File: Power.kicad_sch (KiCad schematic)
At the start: 0 parts

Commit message: added  power components
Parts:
- added U2: LM2776, Package_TO_SOT_SMD:SOT-23-6, symbol Regulator_SwitchedCapacitor:LM2776
- added U5: LM337L_SO8, Package_SO:SOIC-8_3.9x4.9mm_P1.27mm, symbol Regulator_Linear:LM337L_SO8
- added U6: LM1117MP-3.3, Package_TO_SOT_SMD:SOT-223-3_TabPin2, symbol Regulator_Linear:LM1117MP-3.3
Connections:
- new net: U5.2 (VI), U5.3 (VI), U5.6 (VI), U5.7 (VI)
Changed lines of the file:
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@@
 	(generator_version "8.0")
 	(paper "A4")
+	(symbol
+		(lib_id "Regulator_Linear:LM337L_SO8")
+		(at 139.7 92.71 0)
+		(unit 1)
+		(exclude_from_sim no)
+		(in_bom yes)
+		(on_board yes)
+		(dnp no)
+		(fields_autoplaced yes)
+		(property "Reference" "U5"
+			(at 139.7 96.52 0)
+			(effects
+				(font
+					(size 1.27 1.27)
+				)
+			)
+		)
+		(property "Value" "LM337L_SO8"
+			(at 139.7 99.06 0)
+			(effects
+				(font
+					(size 1.27 1.27)
+				)
+			)
+		)
+		(property "Footprint" "Package_SO:SOIC-8_3.9x4.9mm_P1.27mm"
+			(at 139.7 97.79 0)
+			(effects
+				(font
+					(size 1.27 1.27)
+					(italic yes)
+				)
+				(hide yes)
+			)
+		)
+		(property "Datasheet" "http://www.ti.com/lit/ds/symlink/lm337l.pdf"
+			(at 139.7 92.71 0)
+			(effects
+				(font
+					(size 1.27 1.27)
+				)
+				(hide yes)
+			)
+		)
+		(property "Description" "100mA 35V Adjustable Negative Linear Regulator, SO-8"
+			(at 139.7 92.71 0)
+			(effects
+				(font
+					(size 1.27 1.27)
+				)
+				(hide yes)
+			)
+		)
+		(pin "3"
+		)
+		(pin "4"
+		)
+		(pin "2"
+		)
+		(pin "6"
+		)
+		(pin "7"
+		)
+		(pin "8"
+		)
+		(pin "1"
+		)
+		(pin "5"
+		)
+		(instances
+			(project "STM32_Play_Board"
+				(path "/9848a691-cd53-4e57-940a-e5db2e63f9a1/fed4e8b7-2c37-42f6-8803-c612b1069bda"
+					(reference "U5")
+					(unit 1)
+				)
+			)
+		)
+	)
+	(symbol
+		(lib_id "Regulator_Linear:LM1117MP-3.3")
+		(at 99.06 58.42 0)
+		(unit 1)
+		(exclude_from_sim no)
+		(in_bom yes)
+		(on_board yes)
+		(dnp no)
+		(fields_autoplaced yes)
+		(property "Reference" "U6"
+			(at 99.06 52.07 0)
+			(effects
+				(font
+					(size 1.27 1.27)
+				)
+			)
+		)
+		(property "Value" "LM1117MP-3.3"
+			(at 99.06 54.61 0)
+			(effects
+				(font
+					(size 1.27 1.27)
+				)
+			)
+		)
+		(property "Footprint" "Package_TO_SOT_SMD:SOT-223-3_TabPin2"
+			(at 99.06 58.42 0)
+			(effects
+				(font
+					(size 1.27 1.27)
+				)
+				(hide yes)
+			)
+		)
+		(property "Datasheet" "http://www.ti.com/lit/ds/symlink/lm1117.pdf"
+			(at 99.06 58.42 0)
+			(effects
+				(font
+					(size 1.27 1.27)
+				)
+				(hide yes)
+			)
+		)
+		(property "Description" "800mA Low-Dropout Linear Regulator, 3.3V fixed output, SOT-223"
+			(at 99.06 58.42 0)
+			(effects
+				(font
+					(size 1.27 1.27)
+				)
+				(hide yes)
+			)
+		)
+		(pin "1"
+		)
+		(pin "2"
+		)
+		(pin "3"
+		)
+		(instances
+			(project "STM32_Play_Board"
+				(path "/9848a691-cd53-4e57-940a-e5db2e63f9a1/fed4e8b7-2c37-42f6-8803-c612b1069bda"
+					(reference "U6")
+					(unit 1)
+				)
+			)
+		)
+	)
+	(symbol
+		(lib_id "Regulator_SwitchedCapacitor:LM2776")
+		(at 105.41 92.71 0)
+		(unit 1)
+		(exclude_from_sim no)
+		(in_bom yes)
+		(on_board yes)
+		(dnp no)
+		(fields_autoplaced yes)
+		(property "Reference" "U2"
+			(at 118.11 83.8514 0)
+			(effects
+				(font
+					(size 1.27 1.27)
+				)
+			)
+		)
+		(property "Value" "LM2776"
+			(at 118.11 86.3914 0)
+			(effects
+				(font
+					(size 1.27 1.27)
+				)
+			)
+		)
+		(property "Footprint" "Package_TO_SOT_SMD:SOT-23-6"
+			(at 106.68 101.6 0)
+			(effects
+				(font
+					(size 1.27 1.27)
+				)
+				(justify left)
+				(hide yes)
+			)
+		)
+		(property "Datasheet" "http://www.ti.com/lit/ds/symlink/lm2776.pdf"
+			(at 58.42 60.96 0)
+			(effects
+				(font
+					(size 1.27 1.27)
+				)
+				(hide yes)
+			)
+		)
+		(property "Description" "Switched capacitor inverter, inverts positive voltage +2.7 to +5.5V to negative, 200mA, SOT-23-6"
+			(at 105.41 92.71 0)
+			(effects
+				(font
+					(size 1.27 1.27)
+				)
+				(hide yes)
+			)
+		)
+		(pin "1"
+		)
+		(pin "2"
+		)
+		(pin "3"
+		)
+		(pin "5"
+		)
+		(pin "4"
+		)
+		(pin "6"
+		)
+		(instances
+			(project "STM32_Play_Board"
+				(path "/9848a691-cd53-4e57-940a-e5db2e63f9a1/fed4e8b7-2c37-42f6-8803-c612b1069bda"
+					(reference "U2")
+					(unit 1)
+				)
+			)
+		)
+	)
 )

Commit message: dfvdfv
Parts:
- removed U5: LM337L_SO8, Package_SO:SOIC-8_3.9x4.9mm_P1.27mm, symbol Regulator_Linear:LM337L_SO8
- added C15, C16, C18, C6: 10 uF, symbol Device:C
- added C17: 1 uF, symbol Device:C
- added C7: 4.7 uF, symbol Device:C
- added J5, J6: Conn_01x01_Pin, symbol Connector:Conn_01x01_Pin
- added JP1, JP2: Jumper_2_Open, symbol Jumper:Jumper_2_Open
- added R10: 400, symbol Device:R_US
- added R9: 240, symbol Device:R_US
- added U7: LM337L_SO8, Package_SO:SOIC-8_3.9x4.9mm_P1.27mm, symbol Regulator_Linear:LM337L_SO8
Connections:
- net Earth: now reaches U6.1 (GND)
- net Earth: now also U2.2 (GND), C16.2, C17.2, C18.1, C6.2, C7.2, J5.1 (Pin_1), R10.1
- net +3.3V: now reaches U6.2 (VO)
- net +3.3V: now also U2.3 (VIN), U2.4 (EN), C17.1, C6.1
- net at U6.3 (VI): now also C7.1, JP1.2 (B), JP2.2 (B)
- net at U2.1 (VOUT): now also C16.1, U7.2 (VI), U7.3 (VI), U7.6 (VI), U7.7 (VI)
- net at U2.5 (C1+): now also C15.1
- net at U2.6 (C1-): now also C15.2
- new net: J6.1 (Pin_1), JP2.1 (A)
- new net: C18.2, R9.2, U7.1 (VO)
- new net: R10.2, R9.1, U7.4 (ADJ)
- new net VBUS: JP1.1 (A)
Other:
- moved on the sheet: U2, U6

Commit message: added voltage measurement and current measurement
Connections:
- net -3V3: now reaches C18.2, R9.2, U7.1 (VO)
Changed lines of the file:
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@@
+	)
+	(junction
+		(at 214.63 113.03)
+		(diameter 0)
+		(color 0 0 0 0)
 	)
 	(junction
@@
 		(pts
 			(xy 137.16 82.55) (xy 137.16 105.41)
+		)
+		(stroke
+			(width 0)
+			(type default)
+		)
+	)
+	(wire
+		(pts
+			(xy 214.63 113.03) (xy 214.63 120.65)
 		)
 		(stroke
@@
 					(unit 1)
 				)
+			)
+		)
+	)
+	(symbol
+		(lib_id "power:-3V3")
+		(at 214.63 120.65 180)
+		(unit 1)
+		(exclude_from_sim no)
+		(in_bom yes)
+		(on_board yes)
+		(dnp no)
+		(fields_autoplaced yes)
+		(property "Reference" "#PWR033"
+			(at 214.63 116.84 0)
+			(effects
+				(font
+					(size 1.27 1.27)
+				)
+				(hide yes)
+			)
+		)
+		(property "Value" "-3V3"
+			(at 214.63 125.73 0)
+			(effects
+				(font
+					(size 1.27 1.27)
+				)
+			)
+		)
+		(property "Footprint" ""
+			(at 214.63 120.65 0)
+			(effects
+				(font
+					(size 1.27 1.27)
+				)
+				(hide yes)
+			)
+		)
+		(property "Datasheet" ""
+			(at 214.63 120.65 0)
+			(effects
+				(font
+					(size 1.27 1.27)
+				)
+				(hide yes)
+			)
+		)
+		(property "Description" "Power symbol creates a global label with name \"-3V3\""
+			(at 214.63 120.65 0)
+			(effects
+				(font
+					(size 1.27 1.27)
+				)
+				(hide yes)
+			)
+		)
+		(pin "1"
+		)
+		(instances
+			(project "STM32_Play_Board"
+				(path "/9848a691-cd53-4e57-940a-e5db2e63f9a1/fed4e8b7-2c37-42f6-8803-c612b1069bda"
+					(reference "#PWR033")
+					(unit 1)
+				)

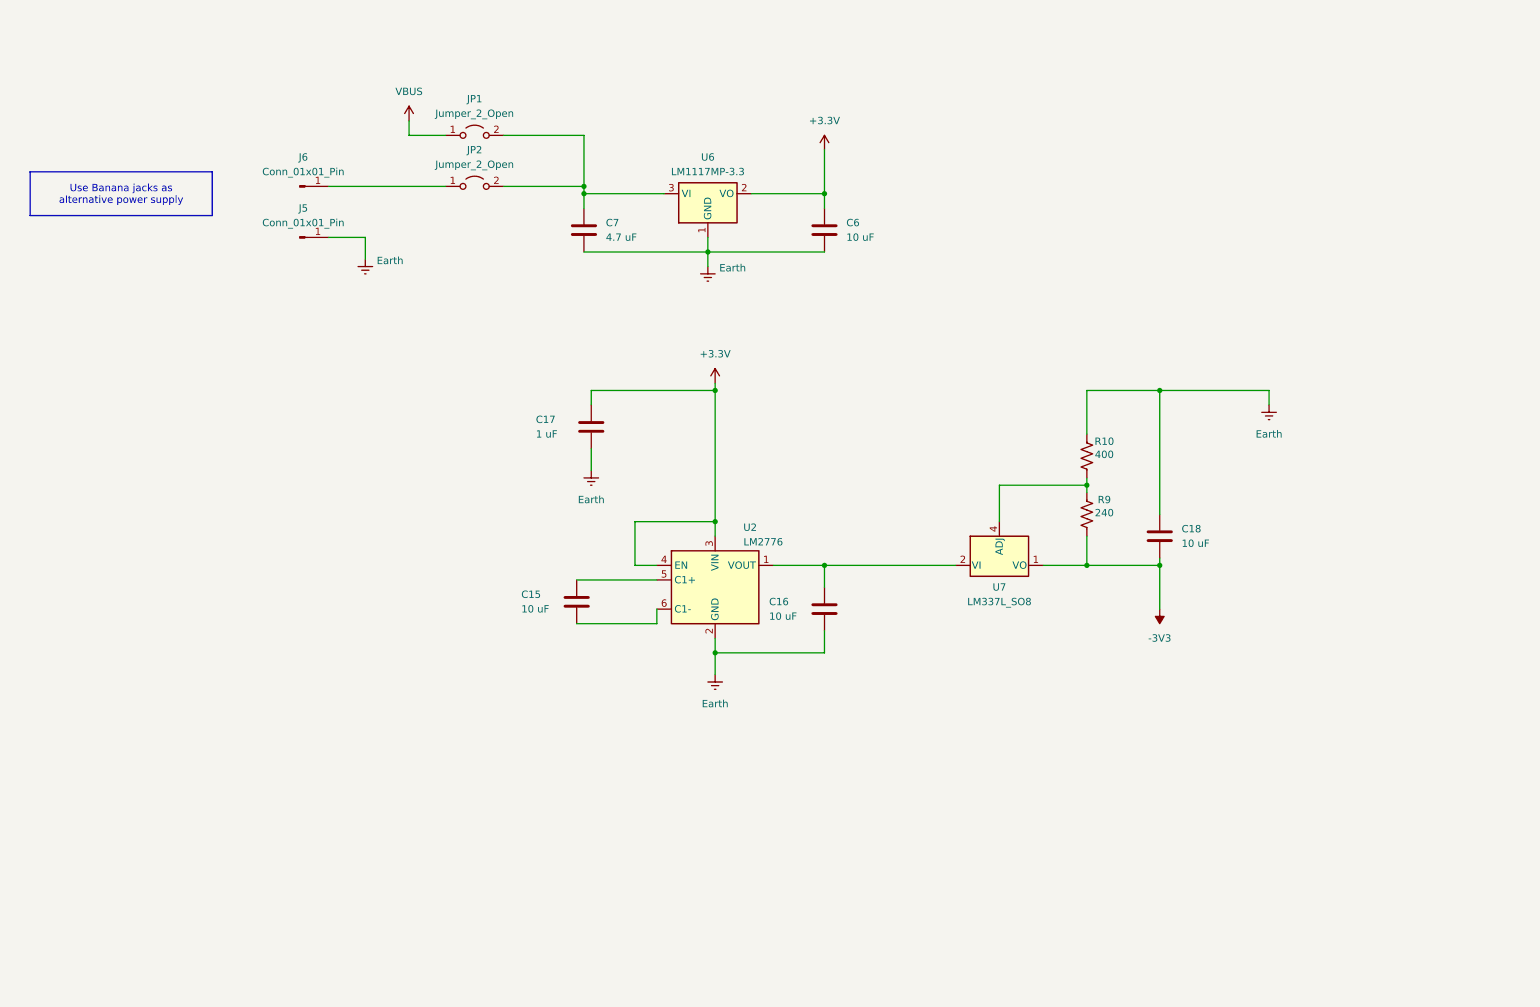
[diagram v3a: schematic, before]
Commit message: updated schematics added the stm cube project file
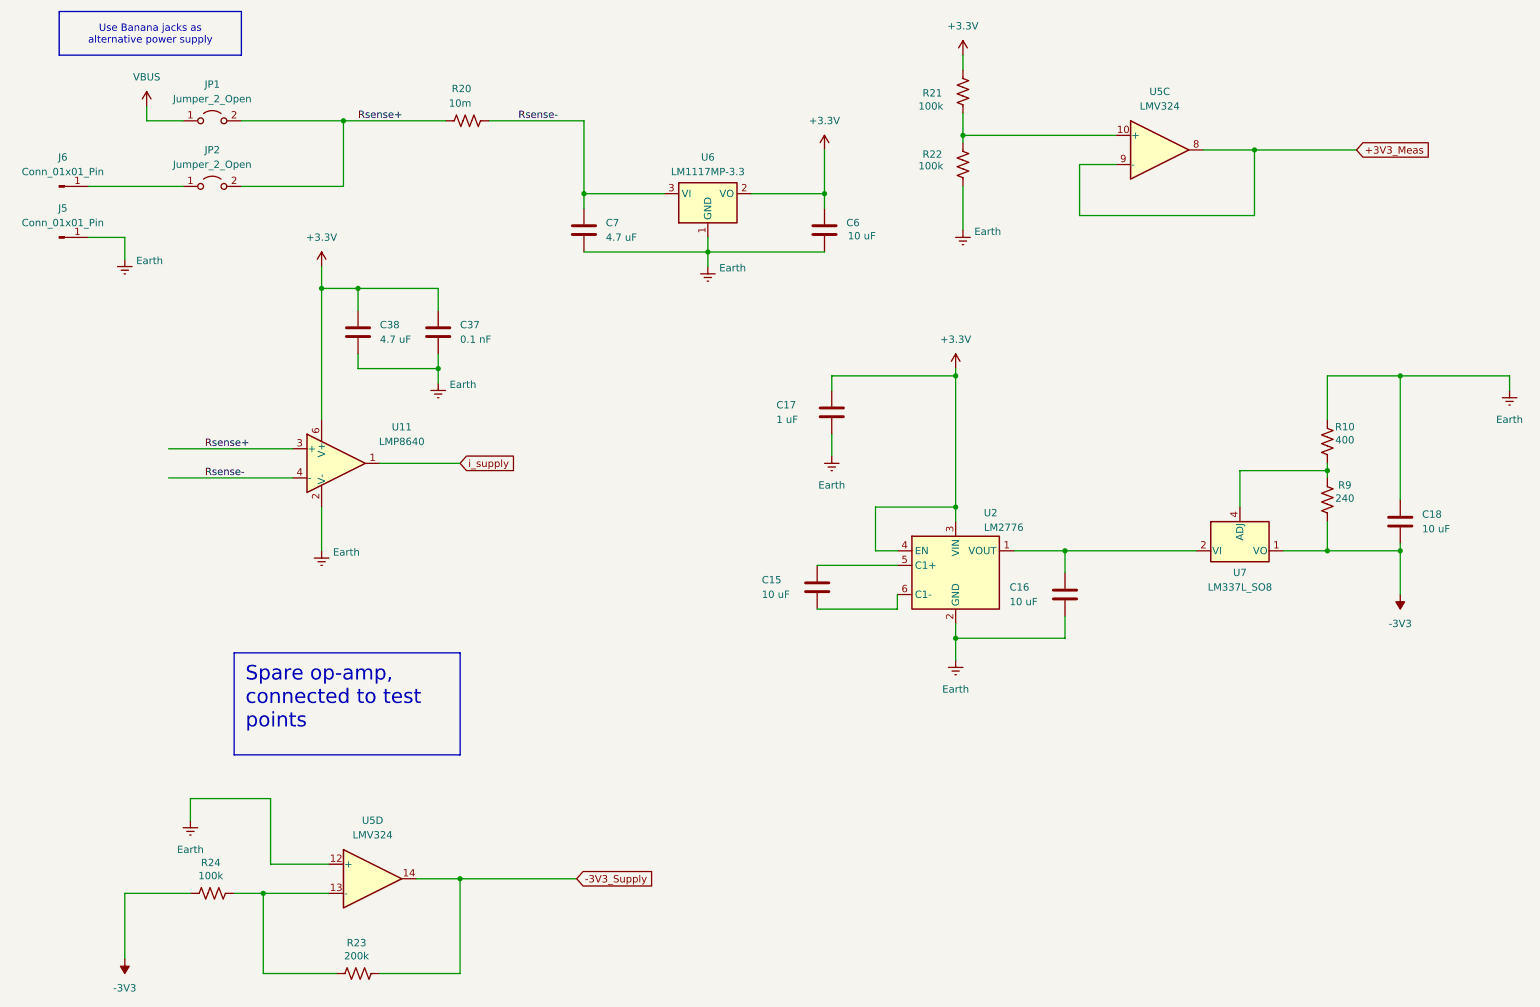
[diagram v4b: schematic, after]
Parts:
- added C37: 0.1 nF, symbol Device:C
- added C38: 4.7 uF, symbol Device:C
- added R20: 10m, symbol Device:R_US
- added R21, R22, R24: 100k, symbol Device:R_US
- added R23: 200k, symbol Device:R_US
- added U11: LMP8640, Package_TO_SOT_SMD:SOT-23-6, symbol Amplifier_Current:LMP8640
- added U5: LMV324, symbol Amplifier_Operational:LMV324
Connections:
- net +3.3V: now also C37.1, C38.1, R21.2, U11.6 (V+)
- net -3V3: now also R24.1
- net Earth: now also C37.2, C38.2, R22.1, U11.2 (V-), U5.12 (+)
- net Rsense+: now reaches JP1.2 (B), JP2.2 (B)
- net Rsense+: now also R20.1, U11.3 (+); no longer C7.1, U6.3 (VI)
- new net: R21.1, R22.2, U5.10 (+)
- new net: R23.1, R24.2, U5.13 (-)
- new net +3V3_Meas: U5.8, U5.9 (-)
- new net -3V3_Supply: R23.2, U5.14
- new net Rsense-: C7.1, R20.2, U11.4 (-), U6.3 (VI)
- new net i_supply: U11.1
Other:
- moved on the sheet: C15, C16, C17, C18, J5, J6, JP1, JP2, R10, R9, U2, U7

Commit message: changes to schematic and PCB
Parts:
- C15, C16, C17, C18, C37, C38, C6, C7: footprint (none) -> Capacitor_SMD:C_0805_2012Metric
- J5: footprint (none) -> TestPoint:TestPoint_THTPad_D1.5mm_Drill0.7mm
- J6: footprint (none) -> TestPoint:TestPoint_THTPad_1.5x1.5mm_Drill0.7mm
- JP1, JP2: footprint (none) -> Connector_PinHeader_2.54mm:PinHeader_1x02_P2.54mm_Vertical
- R10, R20, R21, R22, R23, R24, R9: footprint (none) -> Resistor_SMD:R_0805_2012Metric
- U12: renamed from U5; footprint (none) -> STM32_Play_Board:SOIC-14_3.9x8.7mm_P1.27mm_STM32_Play
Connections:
- net i_supply renamed i_Supply
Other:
- moved on the sheet: C18
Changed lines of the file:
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@@
 	(wire
 		(pts
-			(xy 256.54 110.49) (xy 256.54 109.22)
+			(xy 256.54 110.49) (xy 256.54 99.06)
 		)
 		(stroke
@@
 	(wire
 		(pts
-			(xy 256.54 101.6) (xy 256.54 80.01)
+			(xy 256.54 91.44) (xy 256.54 80.01)
 		)
 		(stroke
@@
 		)
 	)
-	(global_label "i_supply"
-		(shape input)
-		(at 92.71 95.25 0)
+	(hierarchical_label "-3V3_Supply"
+		(shape passive)
+		(at 113.03 167.64 0)
 		(fields_autoplaced yes)
 		(effects
@@
 			(justify left)
 		)
-		(property "Intersheetrefs" "${INTERSHEET_REFS}"
-			(at 103.3755 95.25 0)
-			(effects
-				(font
-					(size 1.27 1.27)
-				)
-				(justify left)
-				(hide yes)
-			)
-		)
 	)
-	(global_label "+3V3_Meas"
-		(shape input)
+	(hierarchical_label "+3V3_Meas"
+		(shape passive)
 		(at 248.92 40.64 0)
 		(fields_autoplaced yes)
@@
 			(justify left)
 		)
-		(property "Intersheetrefs" "${INTERSHEET_REFS}"
-			(at 262.6699 40.64 0)
-			(effects
-				(font
-					(size 1.27 1.27)
-				)
-				(justify left)
-				(hide yes)
-			)
-		)
 	)
-	(global_label "-3V3_Supply"
-		(shape input)
-		(at 113.03 167.64 0)
+	(hierarchical_label "i_Supply"
+		(shape passive)
+		(at 92.71 95.25 0)
 		(fields_autoplaced yes)
 		(effects
@@
 			(justify left)
 		)
-		(property "Intersheetrefs" "${INTERSHEET_REFS}"
-			(at 128.3521 167.64 0)
-			(effects
-				(font
-					(size 1.27 1.27)
-				)
-				(justify left)
-				(hide yes)
-			)
-		)
 	)
 	(symbol
@@
 			)
 		)
-		(property "Footprint" ""
+		(property "Footprint" "Resistor_SMD:R_0805_2012Metric"
 			(at 179.324 30.226 90)
 			(effects
@@
 			)
 		)
-		(property "Footprint" ""
+		(property "Footprint" "Connector_PinHeader_2.54mm:PinHeader_1x02_P2.54mm_Vertical"
 			(at 49.53 46.99 0)
 			(effects
@@
 			)
 		)
-		(property "Footprint" ""
+		(property "Footprint" "TestPoint:TestPoint_THTPad_D1.5mm_Drill0.7mm"
 			(at 22.86 55.88 0)
 			(effects
@@
 			)
 		)
-		(property "Footprint" ""
+		(property "Footprint" "Capacitor_SMD:C_0805_2012Metric"
 			(at 155.9052 120.65 0)
 			(effects
@@
 	(symbol
 		(lib_id "Device:C")
-		(at 256.54 105.41 0)
+		(at 256.54 95.25 0)
 		(unit 1)
 		(exclude_from_sim no)
@@
 		(fields_autoplaced yes)
 		(property "Reference" "C18"
-			(at 260.35 104.1399 0)
+			(at 260.35 93.9799 0)
 			(effects
 				(font
@@
 		)
 		(property "Value" "10 uF"
-			(at 260.35 106.6799 0)
+			(at 260.35 96.5199 0)
 			(effects
 				(font
@@
 			)
 		)
-		(property "Footprint" ""
-			(at 257.5052 109.22 0)
+		(property "Footprint" "Capacitor_SMD:C_0805_2012Metric"
+			(at 257.5052 99.06 0)
 			(effects
 				(font
@@
 		)
 		(property "Datasheet" "~"
-			(at 256.54 105.41 0)
+			(at 256.54 95.25 0)
 			(effects
 				(font
@@
 		)
 		(property "Description" "Unpolarized capacitor"
-			(at 256.54 105.41 0)
+			(at 256.54 95.25 0)
 			(effects
 				(font
@@
 			)
 		)
-		(property "Footprint" ""
+		(property "Footprint" "Capacitor_SMD:C_0805_2012Metric"
 			(at 75.8952 76.2 0)
 			(effects
@@
 			)
 		)
-		(property "Footprint" ""
+		(property "Footprint" "Capacitor_SMD:C_0805_2012Metric"
 			(at 199.0852 121.92 0)
 			(effects
@@
 			)
 		)
-		(property "Footprint" ""
+		(property "Footprint" "Resistor_SMD:R_0805_2012Metric"
 			(at 244.856 101.854 90)
 			(effects
@@
 			)
 		)
-		(property "Footprint" ""
+		(property "Footprint" "TestPoint:TestPoint_THTPad_1.5x1.5mm_Drill0.7mm"
 			(at 22.86 46.99 0)
 			(effects
@@
 			)
 		)
-		(property "Footprint" ""
+		(property "Footprint" "Capacitor_SMD:C_0805_2012Metric"
 			(at 157.1752 58.42 0)
 			(effects
@@
 			)
 		)
-		(property "Footprint" ""
+		(property "Footprint" "Capacitor_SMD:C_0805_2012Metric"
 			(at 115.2652 58.42 0)
 			(effects
@@
 			)
 		)
-		(property "Footprint" ""
+		(property "Footprint" "Resistor_SMD:R_0805_2012Metric"
 			(at 94.234 34.544 90)
 			(effects
@@
 			)
 		)
-		(property "Footprint" ""
+		(property "Footprint" "Resistor_SMD:R_0805_2012Metric"
 			(at 179.324 42.926 90)
 			(effects
@@
 			)
 		)
-		(property "Footprint" ""
+		(property "Footprint" "Resistor_SMD:R_0805_2012Metric"
 			(at 244.856 91.694 90)
 			(effects
@@
 		(dnp no)
 		(fields_autoplaced yes)
-		(property "Reference" "U5"
+		(property "Reference" "U12"
 			(at 214.63 30.48 0)
 			(effects
@@
 			)
 		)
-		(property "Footprint" ""
+		(property "Footprint" "STM32_Play_Board:SOIC-14_3.9x8.7mm_P1.27mm_STM32_Play"
 			(at 213.36 38.1 0)
 			(effects
@@
 			(project "STM32_Play_Board"
 				(path "/9848a691-cd53-4e57-940a-e5db2e63f9a1/fed4e8b7-2c37-42f6-8803-c612b1069bda"
-					(reference "U5")
+					(reference "U12")
 					(unit 3)
 				)
@@
 		(dnp no)
 		(fields_autoplaced yes)
-		(property "Reference" "U5"
+		(property "Reference" "U12"
 			(at 77.47 157.48 0)
 			(effects
@@
 			)
 		)
-		(property "Footprint" ""
+		(property "Footprint" "STM32_Play_Board:SOIC-14_3.9x8.7mm_P1.27mm_STM32_Play"
 			(at 76.2 165.1 0)
 			(effects
@@
 			(project "STM32_Play_Board"
 				(path "/9848a691-cd53-4e57-940a-e5db2e63f9a1/fed4e8b7-2c37-42f6-8803-c612b1069bda"
-					(reference "U5")
+					(reference "U12")
 					(unit 4)
 				)
@@
 			)
 		)
-		(property "Footprint" ""
+		(property "Footprint" "Capacitor_SMD:C_0805_2012Metric"
 			(at 89.8652 76.2 0)
 			(effects
@@
 			)
 		)
-		(property "Footprint" ""
+		(property "Footprint" "Capacitor_SMD:C_0805_2012Metric"
 			(at 158.4452 90.17 0)
 			(effects
@@
 			)
 		)
-		(property "Footprint" ""
+		(property "Footprint" "Connector_PinHeader_2.54mm:PinHeader_1x02_P2.54mm_Vertical"
 			(at 49.53 35.56 0)
 			(effects
@@
 			)
 		)
-		(property "Footprint" ""
+		(property "Footprint" "Resistor_SMD:R_0805_2012Metric"
 			(at 49.784 169.164 90)
 			(effects
@@
 			)
 		)
-		(property "Footprint" ""
+		(property "Footprint" "Resistor_SMD:R_0805_2012Metric"
 			(at 75.184 183.134 90)
 			(effects
